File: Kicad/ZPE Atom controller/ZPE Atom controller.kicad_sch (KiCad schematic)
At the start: 44 parts, among them IC1 TC4424AVPA, J1 50 ohm 21 turns, P1 CONN_01X18, P2 CONN_01X18, Q1 2N2222, Q2 IRF3205, SW1 ON/OFF, SW2 SW_SPST, SW3 SW_SPST, SW4 SW_SPST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

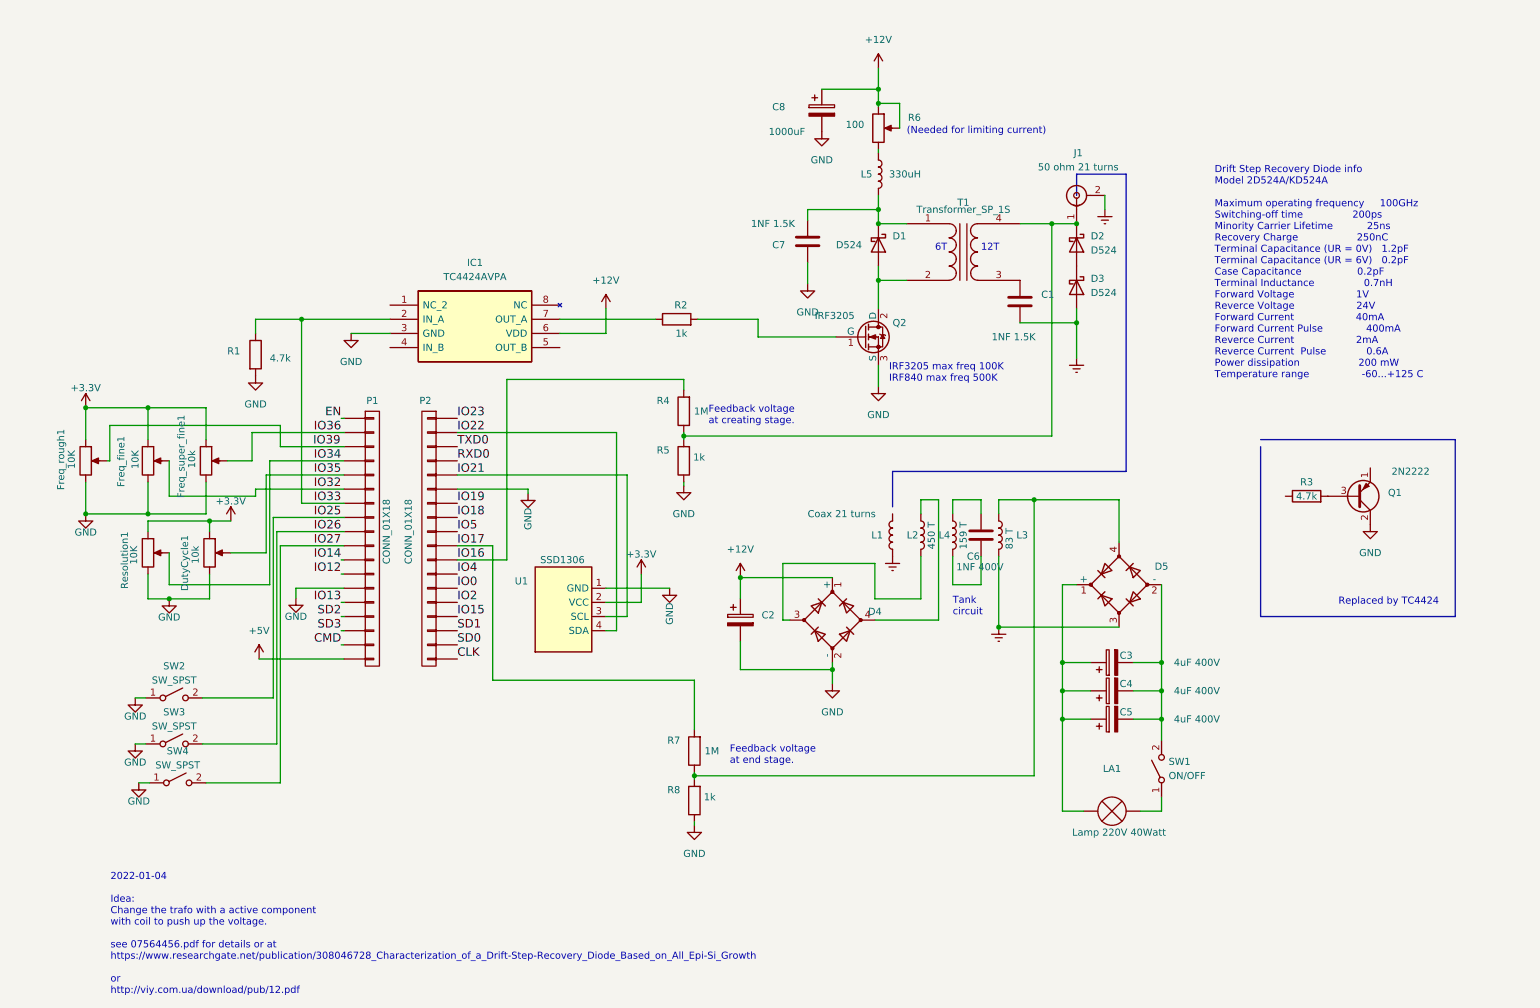
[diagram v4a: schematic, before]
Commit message: Added AC level convert on inputs
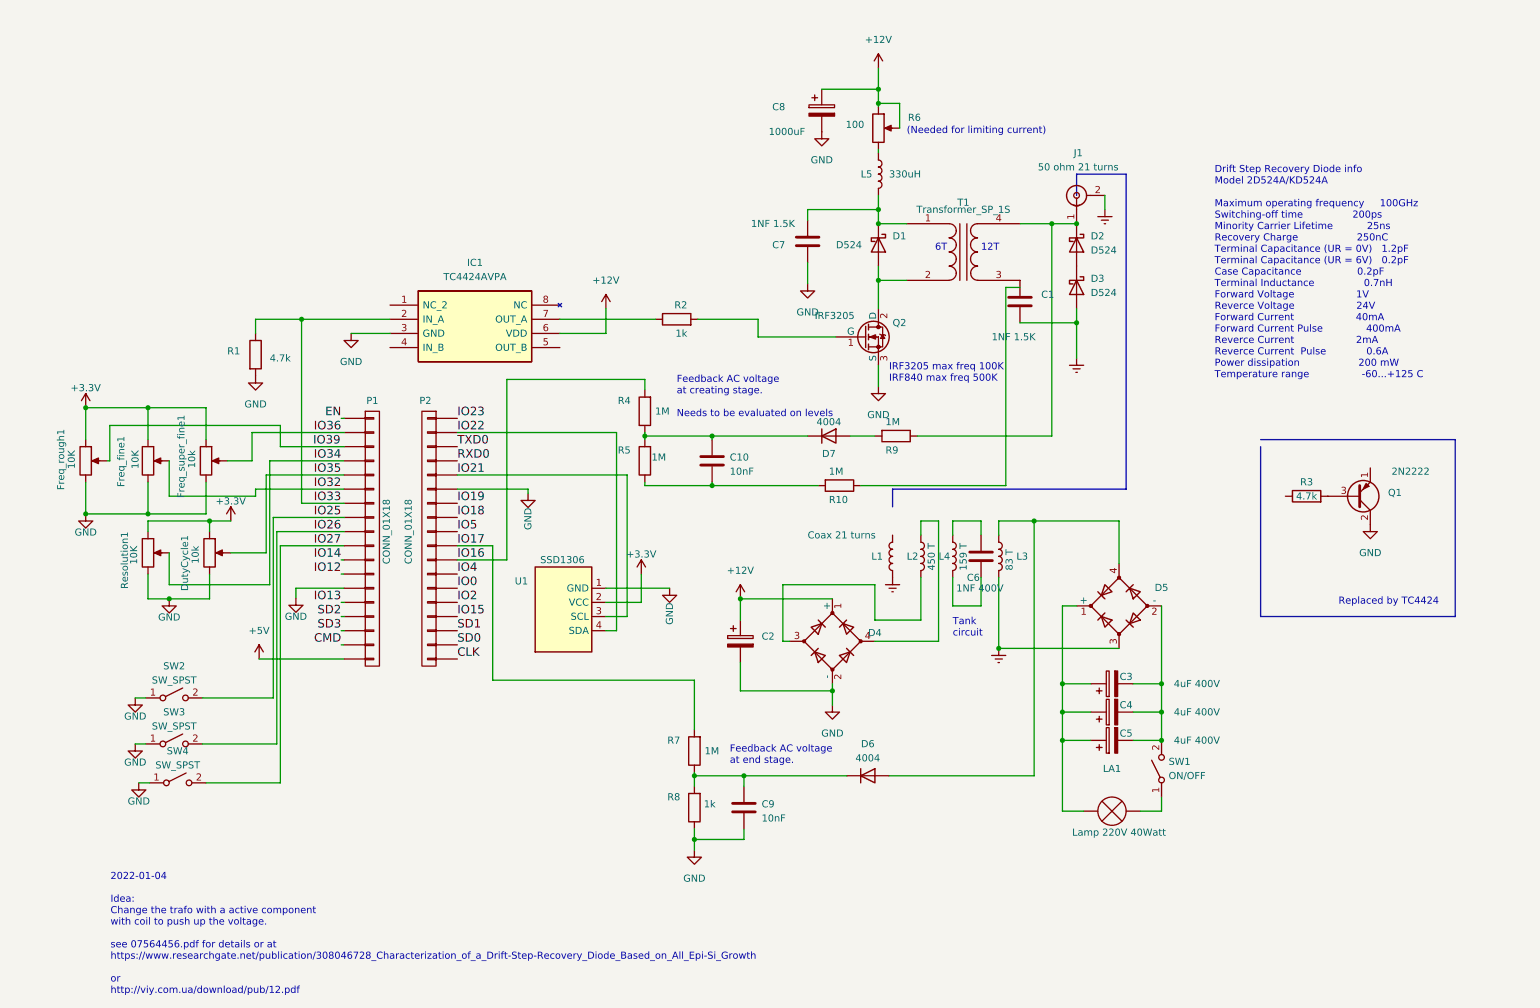
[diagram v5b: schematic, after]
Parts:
- added C10, C9: 10nF, Capacitor_THT:C_Disc_D5.0mm_W2.5mm_P5.00mm, symbol Device:C
- added D6, D7: 4004, Diode_SMD:D_MELF, symbol Device:D
- added R10, R9: 1M, Resistor_THT:R_Axial_DIN0207_L6.3mm_D2.5mm_P10.16mm_Horizontal, symbol Device:R
- C6: footprint (none) -> Capacitor_THT:C_Disc_D5.0mm_W2.5mm_P5.00mm
- R5: value 1k -> 1M
- R6: footprint Potentiometer_THT:Potentiometer_Piher_PC-16_Single_Vertical -> Potentiometer_THT:Potentiometer_Piher_T-16L_Single_Vertical_Hole
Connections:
- net GND: now also C9.2; no longer R5.1
- net at D5.4, L3.2: now also D6.2 (A); no longer R7.1, R8.2
- net at D2.1 (K), J1.1 (In), T1.4 (SB): now also R9.1; no longer R4.1, R5.2
- new net: C10.2, R10.2, R5.1
- new net: C10.1, D7.1 (K), R4.1, R5.2
- new net: C9.1, D6.1 (K), R7.1, R8.2
- new net: D7.2 (A), R9.2
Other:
- note added: "Feedback AC voltage at creating stage. Needs to be evaluated on levels"
- note added: "Feedback AC voltage at end stage."
- note removed: "Feedback voltage at creating stage."
- note removed: "Feedback voltage at end stage."
- title: ZPE Atom controller -> ZPE controller
- moved on the sheet: C2, C3, C4, C5, C6, D4, D5, L1, L2, L3, L4, R4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

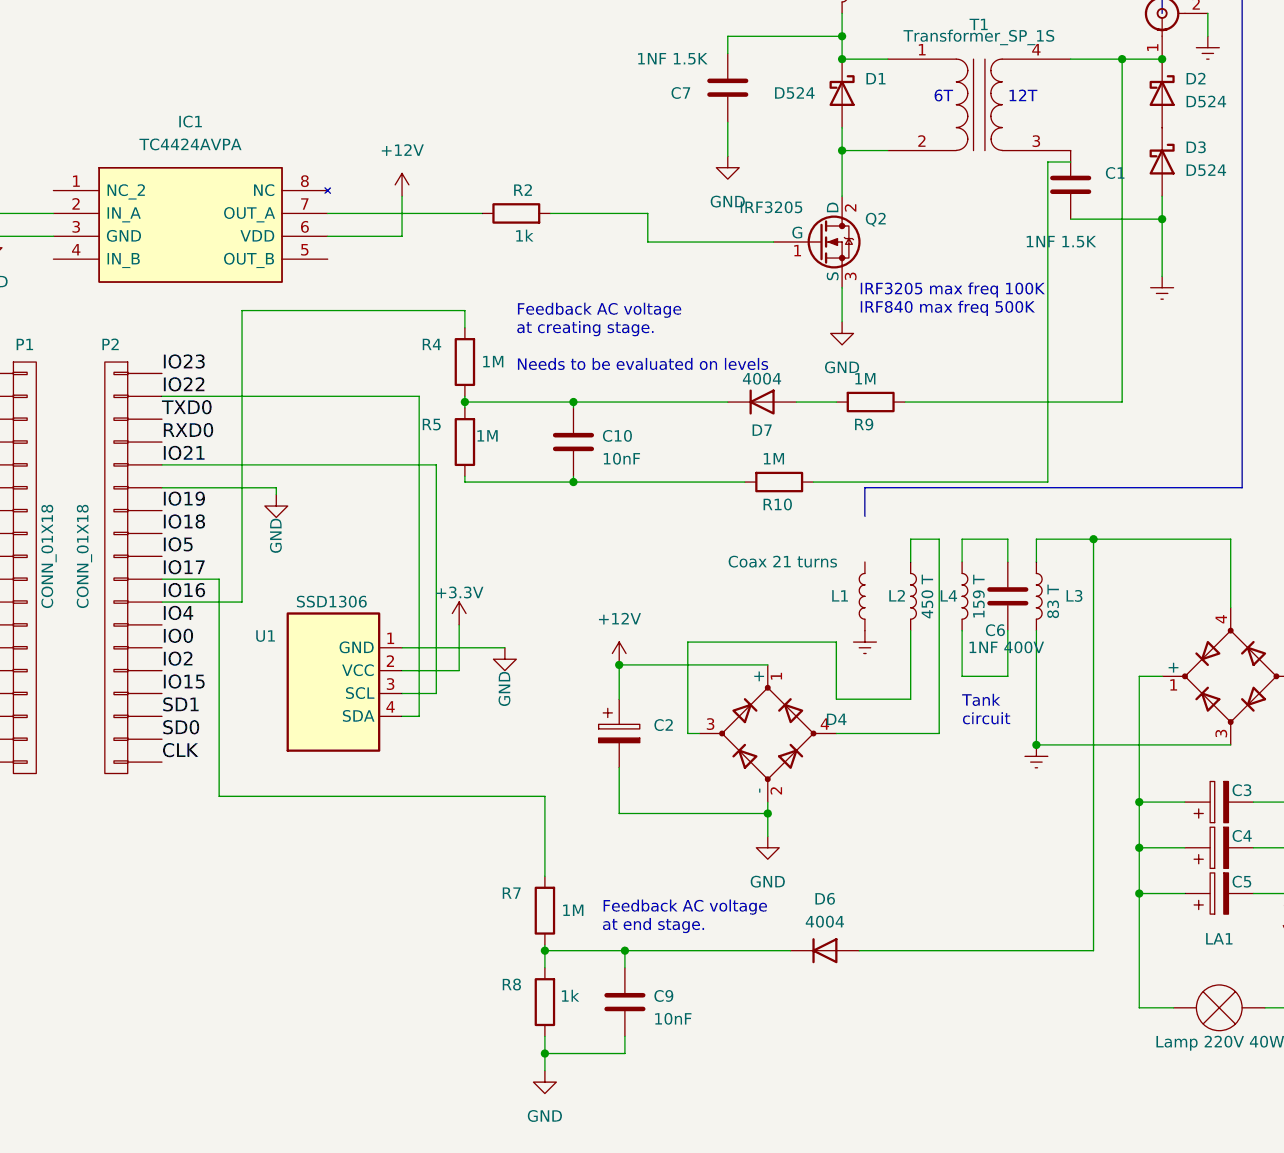
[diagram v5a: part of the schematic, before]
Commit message: Changed pins for feedback to prin 18 and 19
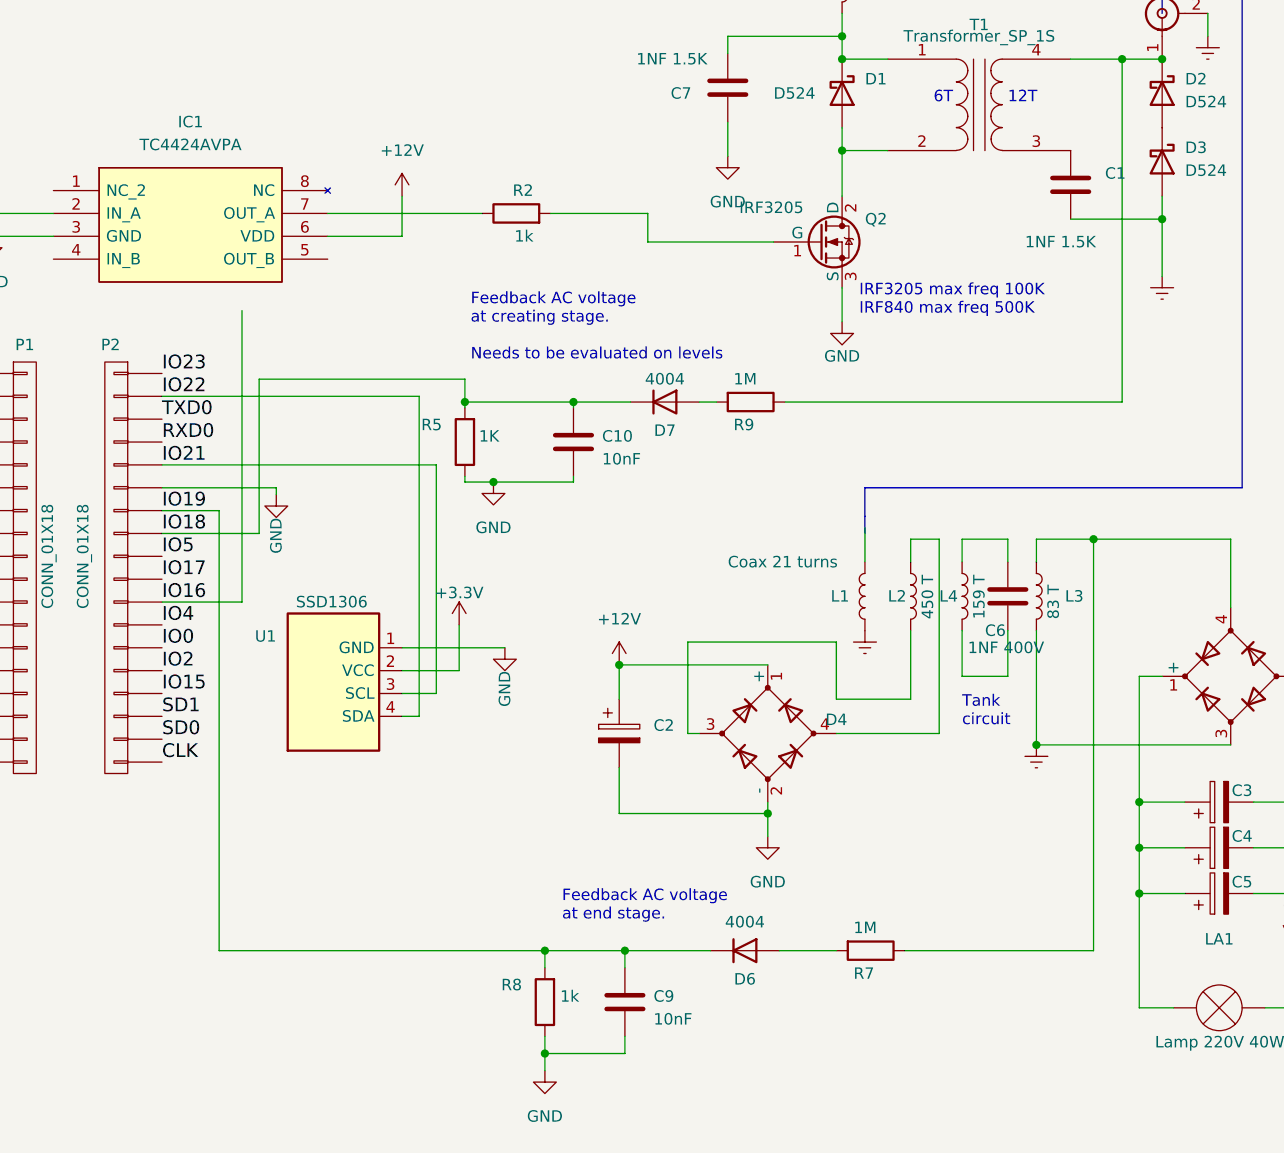
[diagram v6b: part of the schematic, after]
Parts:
- removed R10, R4: 1M, Resistor_THT:R_Axial_DIN0207_L6.3mm_D2.5mm_P10.16mm_Horizontal, symbol Device:R
- R5: value 1M -> 1K
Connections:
- net GND: now also C10.2, R5.1
- net IO17: no longer R7.2
- net IO18: now also C10.1, D7.1 (K), R5.2
- net IO19: now also C9.1, D6.1 (K), R8.2
- net at D5.4, L3.2: now also R7.1; no longer D6.2 (A)
- new net: D6.2 (A), R7.2
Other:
- moved on the sheet: D6, D7, R7, R9

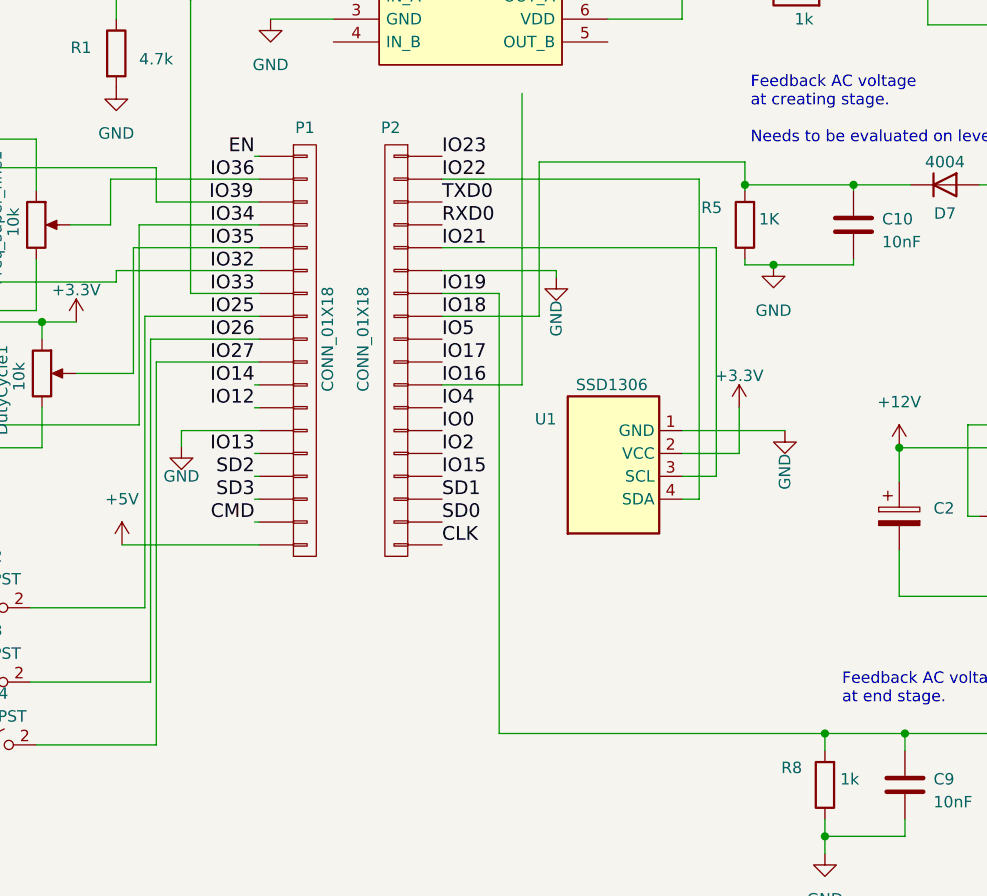
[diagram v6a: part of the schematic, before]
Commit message: Changed feedback pins to 12 and 14
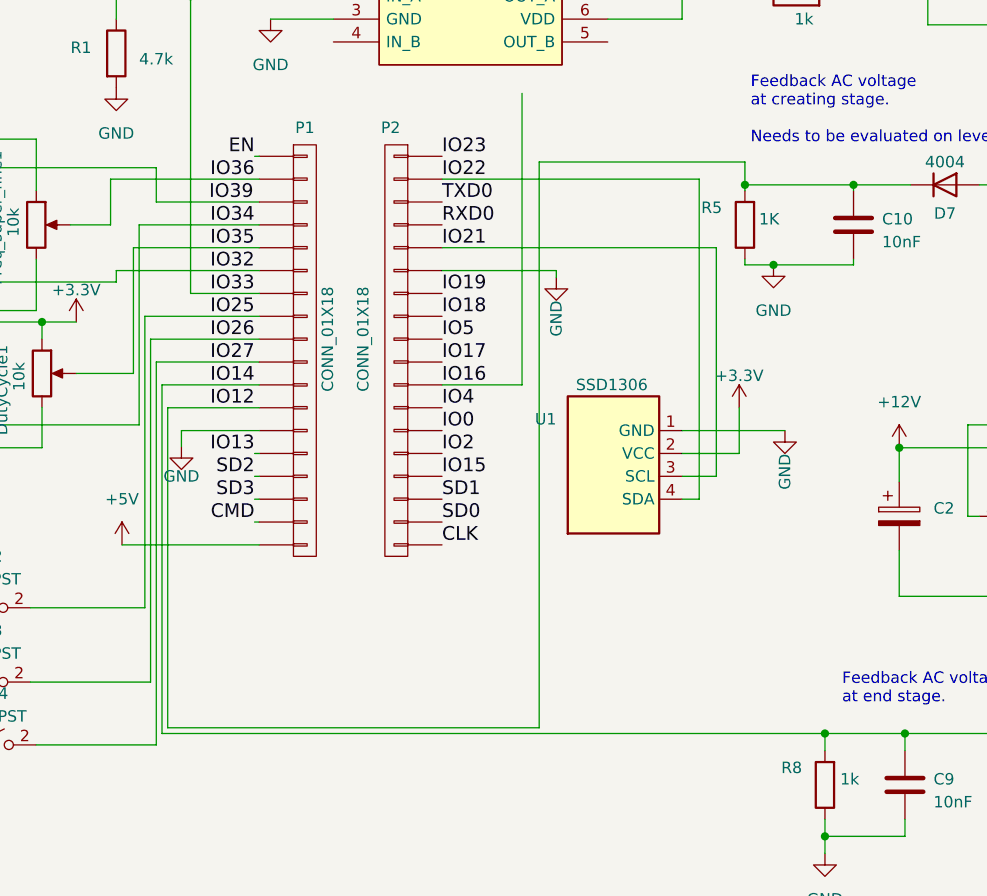
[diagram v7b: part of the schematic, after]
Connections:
- net IO12: now also C10.1, D7.1 (K), R5.2
- net IO14: now also C9.1, D6.1 (K), R8.2
- net IO18: no longer C10.1, D7.1 (K), R5.2
- net IO19: no longer C9.1, D6.1 (K), R8.2
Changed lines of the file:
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@@
+    (stroke (width 0) (type default))
+  )
+  (wire (pts (xy 64.135 147.32) (xy 64.135 111.76))
     (stroke (width 0) (type default))
   )
@@
     (stroke (width 0) (type default))
   )
-  (wire (pts (xy 100.965 99.06) (xy 94.615 99.06))
-    (stroke (width 0) (type default))
-  )
   (wire (pts (xy 169.545 113.665) (xy 153.035 113.665))
     (stroke (width 0) (type default))
@@
     (stroke (width 0) (type default))
   )
-  (wire (pts (xy 100.965 99.06) (xy 100.965 147.955))
-    (stroke (width 0) (type default))
-  )
   (wire (pts (xy 153.035 113.665) (xy 153.035 123.825))
     (stroke (width 0) (type default))
@@
     (stroke (width 0) (type default))
   )
-  (wire (pts (xy 105.41 84.455) (xy 105.41 101.6))
-    (stroke (width 0) (type default))
-  )
   (wire (pts (xy 203.2 141.605) (xy 203.2 136.525))
     (stroke (width 0) (type default))
@@
     (stroke (width 0) (type default))
   )
+  (wire (pts (xy 63.5 109.22) (xy 74.295 109.22))
+    (stroke (width 0) (type default))
+  )
   (wire (pts (xy 39.116 116.205) (xy 39.116 111.76))
     (stroke (width 0) (type default))
@@
     (stroke (width 0) (type default))
   )
-  (wire (pts (xy 100.965 147.955) (xy 137.16 147.955))
+  (wire (pts (xy 63.5 147.955) (xy 137.16 147.955))
     (stroke (width 0) (type default))
   )
@@
     (stroke (width 0) (type default))
   )
+  (wire (pts (xy 64.135 111.76) (xy 74.295 111.76))
+    (stroke (width 0) (type default))
+  )
   (wire (pts (xy 148.59 66.04) (xy 148.59 69.215))
     (stroke (width 0) (type default))
@@
     (stroke (width 0) (type default))
   )
-  (wire (pts (xy 74.295 111.76) (xy 73.787 111.76))
-    (stroke (width 0) (type default))
-  )
   (wire (pts (xy 170.18 20.955) (xy 170.18 24.765))
     (stroke (width 0) (type default))
@@
     (stroke (width 0) (type default))
   )
-  (wire (pts (xy 105.41 101.6) (xy 94.615 101.6))
-    (stroke (width 0) (type default))
-  )
   (wire (pts (xy 57.785 86.36) (xy 57.785 91.44))
     (stroke (width 0) (type default))
@@
     (stroke (width 0) (type default))
   )
-  (wire (pts (xy 74.295 109.22) (xy 73.787 109.22))
+  (wire (pts (xy 63.5 147.955) (xy 63.5 109.22))
     (stroke (width 0) (type default))
   )
@@
     (stroke (width 0) (type default))
   )
+  (wire (pts (xy 105.41 147.32) (xy 64.135 147.32))
+    (stroke (width 0) (type default))
+  )
   (wire (pts (xy 39.116 81.915) (xy 39.116 87.63))
     (stroke (width 0) (type default))
@@
     (stroke (width 0) (type default))
   )
+  (wire (pts (xy 105.41 84.455) (xy 105.41 147.32))
+    (stroke (width 0) (type default))
+  )
